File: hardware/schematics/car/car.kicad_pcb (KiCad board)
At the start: 12 copper layers, 53.3 x 107.8 mm, 22 parts, among them M1 Motor_Servo, Q1 PMOS, SW1 SW_SPST, SW2 SW_Push, SW3 SW_Push, U1 VL53L0CXV0DH1, U10 Mini-560, U11 JGA25-37x, U2 VL53L0CXV0DH1, U3 VL53L0CXV0DH1, U4 Pixy2, U6 TB6612FNG, U7 SparkFun OTOS, U9 Mini-360

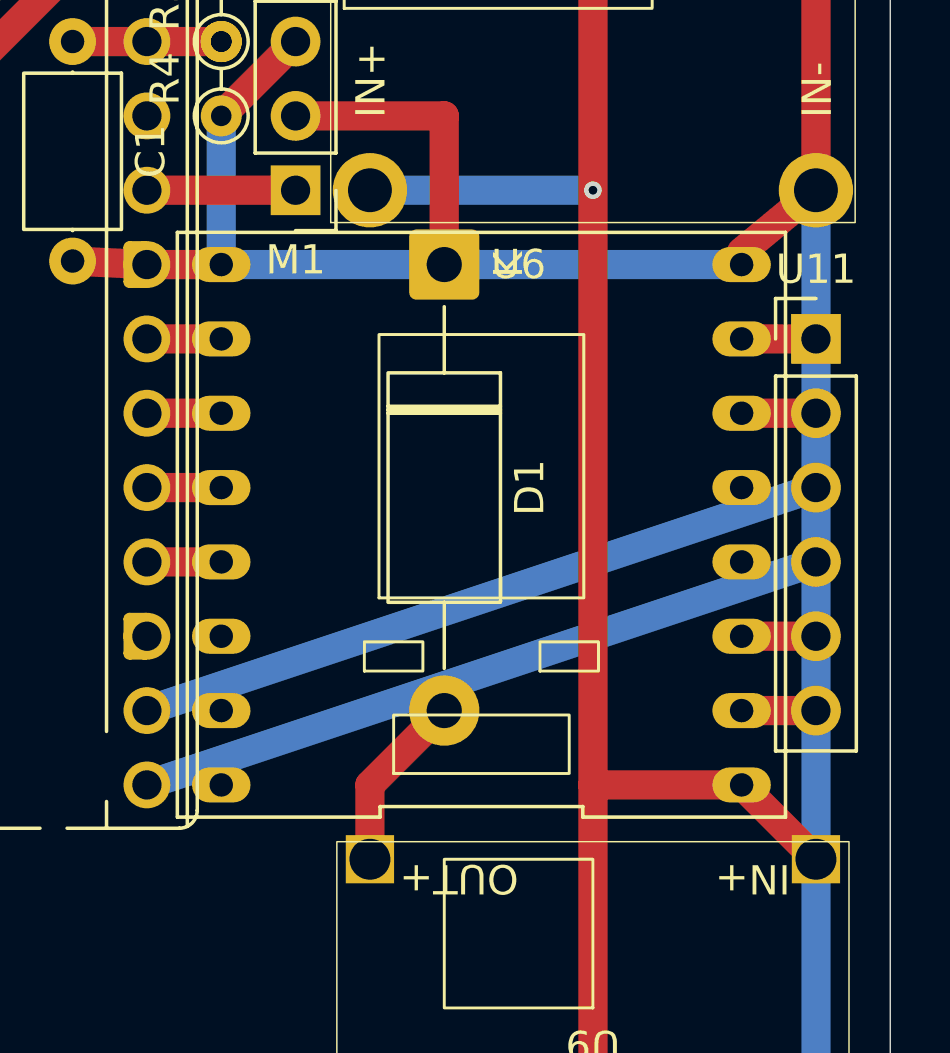
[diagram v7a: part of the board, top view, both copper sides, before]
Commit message: [Schematic] reroute the fixed footprint.
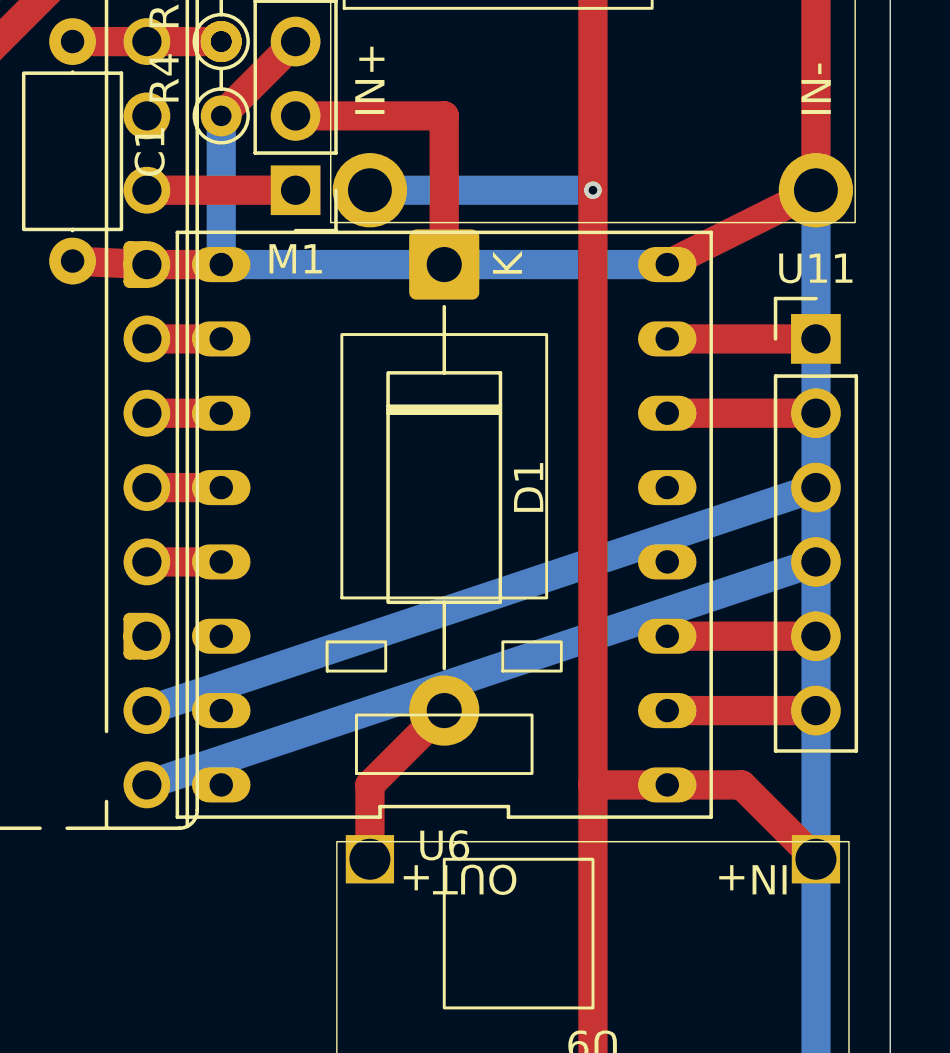
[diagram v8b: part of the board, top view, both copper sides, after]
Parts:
- moved U6 1.27 mm to (154.9, 54.6)
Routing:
- net +3.3V: track 81.2 -> 91.3 mm
- net Net-(U11-M2): track 2.54 -> 5.08 mm
- net Net-(U11-M1): track 2.54 -> 5.08 mm
- net GND: track 333.3 -> 335.7 mm
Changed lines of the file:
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@@
 	(footprint "xlnc-foot:TB6612FNG_Breakout_Sparkfun"
 		(layer "F.Cu")
-		(at 156.21 54.61 90)
+		(at 154.94 54.61 90)
 		(tags "TB6612FNG, driver motor")
 		(property "Reference" "U6"
-			(at 8.89 1.27 0)
+			(at -10.99 0 180)
 			(layer "F.SilkS")
 			(effects
@@
 		)
 		(property "Value" "TB6612FNG"
-			(at 11 0 0)
+			(at 11 0 180)
 			(layer "F.Fab")
 			(effects
@@
 			)
 		)
-		(property "Datasheet" "https://toshiba.semicon-storage.com/us/product/linear/motordriver/detail.TB6612FNG.html"
+		(property "Datasheet" ""
 			(at 0 0 90)
 			(layer "F.Fab")
@@
 			)
 		)
-		(property "Description" "Driver IC for Dual DC motor, SSOP-24"
+		(property "Description" ""
 			(at 0 0 90)
 			(layer "F.Fab")
@@
 		(sheetname "/")
 		(sheetfile "car.kicad_sch")
-		(units
-			(unit
-				(name "A")
-				(pins "19" "23" "15" "21" "22" "17" "16" "20" "18" "24" "3" "4" "13"
-					"14" "10" "9" "1" "2" "6" "5" "12" "11" "8" "7"
-				)
-			)
-		)
 		(attr through_hole)
 		(duplicate_pad_numbers_are_jumpers no)
 		(fp_line
-			(start 9.99 -10.39)
-			(end -9.99 -10.39)
+			(start 9.99 -9.12)
+			(end -9.99 -9.12)
 			(stroke
 				(width 0.12)
@@
 		)
 		(fp_line
-			(start -9.99 -10.39)
-			(end -9.99 -3.463333)
+			(start -9.99 -9.12)
+			(end -9.99 -2.193333)
 			(stroke
 				(width 0.12)
-				(type default)
+				(type solid)
 			)
 			(layer "F.SilkS")
 		)
 		(fp_line
-			(start -9.63 -3.463333)
-			(end -9.63 3.463333)
+			(start -9.99 -2.193333)
+			(end -9.63 -2.193333)
 			(stroke
 				(width 0.12)
@@
 		)
 		(fp_line
-			(start -9.99 -3.463333)
-			(end -9.63 -3.463333)
+			(start -9.63 2.193333)
+			(end -9.63 -2.193333)
 			(stroke
 				(width 0.12)
-				(type default)
+				(type solid)
 			)
 			(layer "F.SilkS")
 		)
 		(fp_line
-			(start -9.63 3.463333)
-			(end -9.99 3.463333)
+			(start -9.63 2.193333)
+			(end -9.99 2.193333)
 			(stroke
 				(width 0.12)
@@
 		)
 		(fp_line
-			(start -9.99 3.463333)
-			(end -9.99 10.39)
+			(start -9.99 2.193333)
+			(end -9.99 9.12)
 			(stroke
 				(width 0.12)
@@
 		)
 		(fp_line
-			(start 9.99 10.39)
-			(end 9.99 -10.39)
+			(start 9.99 9.12)
+			(end 9.99 -9.12)
 			(stroke
 				(width 0.12)
-				(type default)
+				(type solid)
 			)
 			(layer "F.SilkS")
 		)
 		(fp_line
-			(start -9.99 10.39)
-			(end 9.99 10.39)
+			(start -9.99 9.12)
+			(end 9.99 9.12)
 			(stroke
 				(width 0.12)
@@
 		)
 		(fp_line
-			(start 9.74 -10.14)
-			(end 9.74 10.14)
+			(start 9.74 -8.87)
+			(end 9.74 8.87)
 			(stroke
 				(width 0.05)
-				(type default)
+				(type solid)
 			)
 			(layer "F.CrtYd")
 		)
 		(fp_line
-			(start -9.74 -10.14)
-			(end 9.74 -10.14)
+			(start -9.74 -8.87)
+			(end 9.74 -8.87)
 			(stroke
 				(width 0.05)
@@
 		)
 		(fp_line
-			(start 9.74 10.14)
-			(end -9.74 10.14)
+			(start 9.74 8.87)
+			(end -9.74 8.87)
 			(stroke
 				(width 0.05)
@@
 		)
 		(fp_line
-			(start -9.74 10.14)
-			(end -9.74 -10.14)
+			(start -9.74 8.87)
+			(end -9.74 -8.87)
 			(stroke
 				(width 0.05)
-				(type default)
+				(type solid)
 			)
 			(layer "F.CrtYd")
 		)
 		(pad "1" thru_hole oval
-			(at -1.27 8.89 90)
+			(at -1.27 7.62 90)
 			(size 1.2 2)
 			(drill 0.8)
@@
 		)
 		(pad "5" thru_hole oval
-			(at 1.27 8.89 90)
+			(at 1.27 7.62 90)
 			(size 1.2 2)
 			(drill 0.8)
@@
 		)
 		(pad "7" thru_hole oval
-			(at 3.81 8.89 90)
+			(at 3.81 7.62 90)
 			(size 1.2 2)
 			(drill 0.8)
@@
 		)
 		(pad "11" thru_hole oval
-			(at 6.35 8.89 90)
+			(at 6.35 7.62 90)
 			(size 1.2 2)
 			(drill 0.8)
@@
 		)
 		(pad "15" thru_hole oval
-			(at 6.35 -8.89 90)
+			(at 6.35 -7.62 90)
 			(size 1.2 2)
 			(drill 0.8)
@@
 		)
 		(pad "16" thru_hole oval
-			(at 3.81 -8.89 90)
+			(at 3.81 -7.62 90)
 			(size 1.2 2)
 			(drill 0.8)
@@
 		)
 		(pad "17" thru_hole oval
-			(at 1.27 -8.89 90)
+			(at 1.27 -7.62 90)
 			(size 1.2 2)
 			(drill 0.8)
@@
 		)
 		(pad "18" thru_hole oval
-			(at -3.81 8.89 90)
+			(at -3.81 7.62 90)
 			(size 1.2 2)
 			(drill 0.8)
@@
 		)
 		(pad "18" thru_hole oval
-			(at 8.89 -8.89 90)
+			(at 8.89 -7.62 90)
 			(size 1.2 2)
 			(drill 0.8)
@@
 		)
 		(pad "18" thru_hole oval
-			(at 8.89 8.89 90)
+			(at 8.89 7.62 90)
 			(size 1.2 2)
 			(drill 0.8)
@@
 		)
 		(pad "19" thru_hole oval
-			(at -1.27 -8.89 90)
+			(at -1.27 -7.62 90)
 			(size 1.2 2)
 			(drill 0.8)
@@
 		)
 		(pad "20" thru_hole oval
-			(at -6.35 8.89 90)
+			(at -6.35 7.62 90)
 			(size 1.2 2)
 			(drill 0.8)
@@
 		)
 		(pad "21" thru_hole oval
-			(at -3.81 -8.89 90)
+			(at -3.81 -7.62 90)
 			(size 1.2 2)
 			(drill 0.8)
@@
 		)
 		(pad "22" thru_hole oval
-			(at -6.35 -8.89 90)
+			(at -6.35 -7.62 90)
 			(size 1.2 2)
 			(drill 0.8)
@@
 		)
 		(pad "23" thru_hole oval
-			(at -8.89 -8.89 90)
+			(at -8.89 -7.62 90)
 			(size 1.2 2)
 			(drill 0.8)
@@
 		)
 		(pad "24" thru_hole oval
-			(at -8.89 8.89 90)
+			(at -8.89 7.62 90)
 			(size 1.2 2)
 			(drill 0.8)
@@
 	)
 	(segment
-		(start 167.64 43.18)
-		(end 165.1 45.285)
-		(width 1)
-		(layer "F.Cu")
-		(net "GND")
-	)
-	(segment
 		(start 122.041139 58.437306)
 		(end 124.46 58.42)
@@
 	)
 	(segment
+		(start 167.64 58.42)
+		(end 162.56 58.42)
+		(width 1)
+		(layer "F.Cu")
+		(net "GND")
+	)
+	(segment
+		(start 167.64 43.18)
+		(end 162.56 45.72)
+		(width 1)
+		(layer "F.Cu")
+		(net "GND")
+	)
+	(segment
 		(start 167.64 15.24)
 		(end 167.64 43.18)
@@
 	)
 	(segment
-		(start 165.1 58.42)
-		(end 167.64 58.42)
-		(width 1)
-		(layer "F.Cu")
-		(net "GND")
-	)
-	(segment
 		(start 124.46 76.2)
 		(end 119.38 76.2)
@@
 	)
 	(segment
-		(start 165.1 45.72)
-		(end 147.32 45.72)
+		(start 167.64 76.2)
+		(end 152.4 75.8)
 		(width 1)
 		(layer "B.Cu")
@@
 	)
 	(segment
-		(start 167.64 76.2)
-		(end 152.4 75.8)
+		(start 162.56 45.72)
+		(end 147.32 45.72)
 		(width 1)
 		(layer "B.Cu")
@@
 	)
 	(segment
+		(start 137.16 33.02)
+		(end 142.24 33.02)
+		(width 1)
+		(layer "F.Cu")
+		(net "Net-(BZ1-+)")
+	)
+	(segment
+		(start 142.24 30.48)
+		(end 144.78 30.48)
+		(width 1)
+		(layer "F.Cu")
+		(net "Net-(A1-GPIO28_ADC2)")
+	)
+	(segment
 		(start 163.93 96.52)
 		(end 165.0975 85.09)
@@
 	)
 	(segment
-		(start 165.1 50.8)
-		(end 167.64 50.8)
+		(start 167.64 50.8)
+		(end 162.56 50.8)
 		(width 1)
 		(layer "F.Cu")
@@
 	)
 	(segment
-		(start 165.1 48.26)
-		(end 167.64 48.26)
+		(start 167.64 48.26)
+		(end 162.56 48.26)
 		(width 1)
 		(layer "F.Cu")
@@
 	)
 	(segment
-		(start 165.1 60.96)
-		(end 167.64 60.96)
+		(start 167.64 60.96)
+		(end 162.56 60.96)
 		(width 1)
 		(layer "F.Cu")
@@
 	)
 	(segment
-		(start 162.56 33.02)
-		(end 144.78 25.4)
+		(start 165.1 60.96)
+		(end 157.48 60.96)
 		(width 1)
 		(layer "In10.Cu")
@@
 	)
 	(segment
-		(start 162.56 58.42)
-		(end 162.56 33.02)
+		(start 157.48 60.96)
+		(end 157.48 25.4)
 		(width 1)
 		(layer "In10.Cu")
@@
 	)
 	(segment
-		(start 165.1 60.96)
-		(end 162.56 58.42)
+		(start 157.48 25.4)
+		(end 144.78 25.4)
 		(width 1)
 		(layer "In10.Cu")
@@
 	)
 	(segment
-		(start 142.24 30.48)
-		(end 144.78 30.48)
-		(width 1)
-		(layer "F.Cu")
-		(net "Net-(A1-GPIO28_ADC2)")
-	)
-	(segment
 		(start 144.78 17.78)
 		(end 147.32 20.32)
@@
 		(net "Net-(D1-K)")
 	)
-	(segment
-		(start 137.16 33.02)
-		(end 142.24 33.02)
-		(width 1)
-		(layer "F.Cu")
-		(net "Net-(BZ1-+)")
-	)
 	(group ""
